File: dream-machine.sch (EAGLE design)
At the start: 8 parts, among them J1 AVR_SPI_PRG_62X3_LOCK, SW1 Now, U1 ATTINY13SOIC

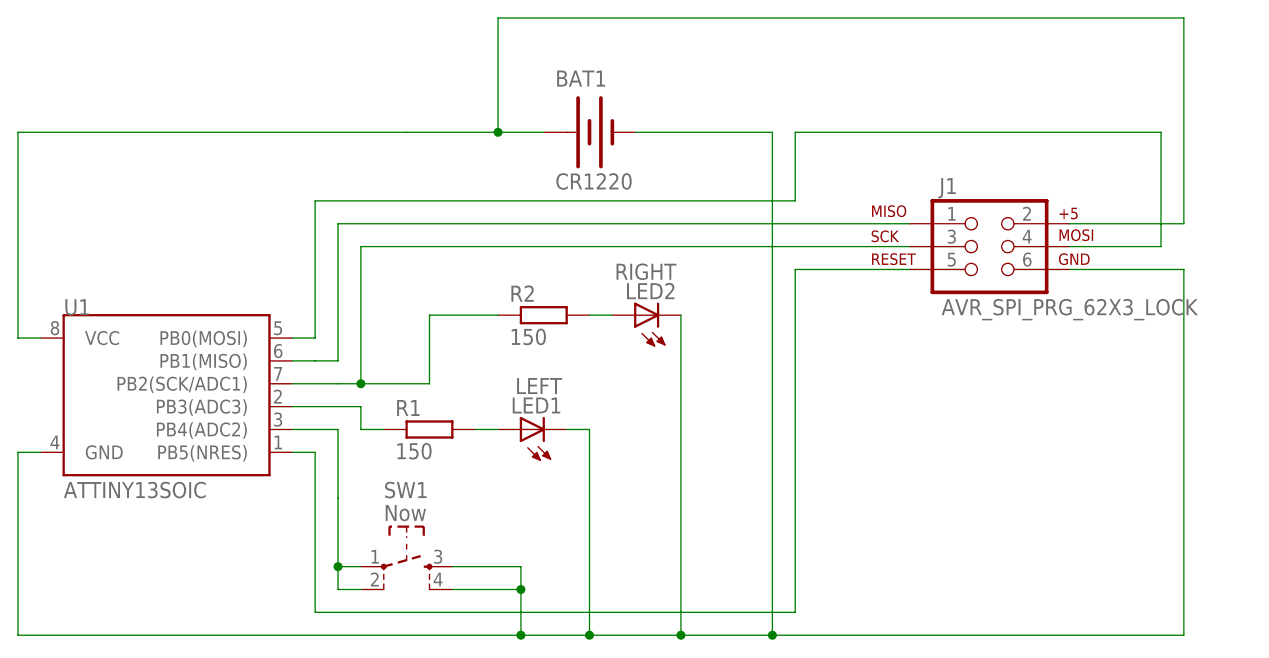
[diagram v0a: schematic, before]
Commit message: Added power jumper. Fixed orientation of battery holder.
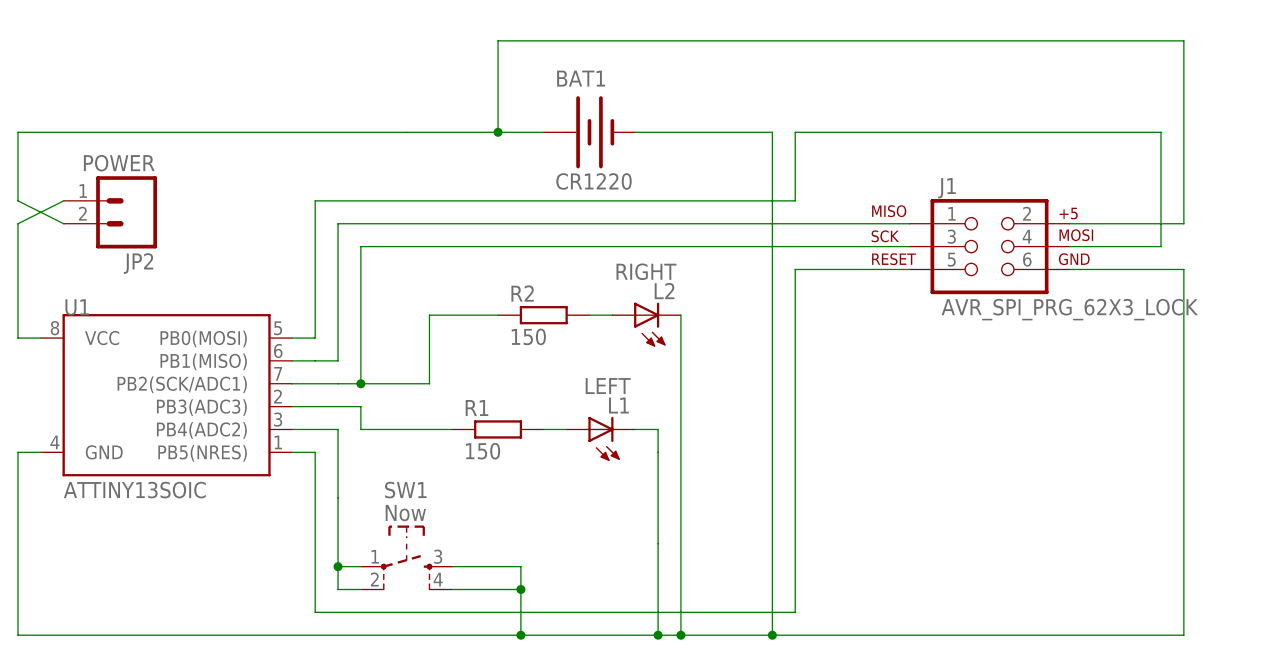
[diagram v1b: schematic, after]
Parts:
- removed LED1: LEFT, dp_devices:LED-3MM
- added JP2: POWER, SparkFun:M02LOCK
- added L1: LEFT, dp_devices:LED-3MM
- renumbered LED2 to L2
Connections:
- new net VCC-POWER: JP2.1, U1.VCC
- net GND: now also L1.C; no longer LED1.C
- net L1-R: now also L1.A; no longer LED1.A
- net VCC: now also JP2.2; no longer U1.VCC
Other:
- moved on the sheet: R1
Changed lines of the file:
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@@
 <part name="U1" library="SparkFun" deviceset="ATTINY13" device="SOIC"/>
 <part name="SW1" library="dp_devices" deviceset="SW_TACT" device="" value="Now"/>
-<part name="LED1" library="dp_devices" deviceset="LED" device="-3MM" value="LEFT"/>
-<part name="LED2" library="dp_devices" deviceset="LED" device="-3MM" value="RIGHT"/>
+<part name="L1" library="dp_devices" deviceset="LED" device="-3MM" value="LEFT"/>
+<part name="L2" library="dp_devices" deviceset="LED" device="-3MM" value="RIGHT"/>
 <part name="R2" library="dp_devices" deviceset="RESISTOR" device="-0805" technology="R805" value="150"/>
 <part name="R1" library="dp_devices" deviceset="RESISTOR" device="-0805" technology="R805" value="150"/>
 <part name="J1" library="SparkFun" deviceset="AVR_SPI_PRG_6" device="2X3_LOCK"/>
+<part name="JP2" library="SparkFun" deviceset="M02" device="LOCK" value="POWER"/>
 </parts>
 <sheets>
@@
 <instance part="U1" gate="G$1" x="27.94" y="35.56"/>
 <instance part="SW1" gate="G$1" x="53.34" y="17.78"/>
-<instance part="LED1" gate="LED" x="66.04" y="33.02" rot="R90"/>
-<instance part="LED2" gate="LED" x="78.74" y="45.72" rot="R90"/>
+<instance part="L1" gate="LED" x="73.66" y="33.02" rot="R90"/>
+<instance part="L2" gate="LED" x="78.74" y="45.72" rot="R90"/>
 <instance part="R2" gate="G$1" x="68.58" y="45.72"/>
-<instance part="R1" gate="G$1" x="55.88" y="33.02"/>
+<instance part="R1" gate="G$1" x="63.5" y="33.02"/>
 <instance part="J1" gate="G$1" x="116.84" y="53.34"/>
+<instance part="JP2" gate="G$1" x="22.86" y="58.42" rot="R180"/>
 </instances>
 <busses>
@@
 <pinref part="BAT1" gate="G$1" pin="+"/>
 <wire x1="68.58" y1="66.04" x2="63.5" y2="66.04" width="0.1524" layer="91"/>
-<pinref part="U1" gate="G$1" pin="VCC"/>
 <wire x1="63.5" y1="66.04" x2="53.34" y2="66.04" width="0.1524" layer="91"/>
-<wire x1="12.7" y1="43.18" x2="10.16" y2="43.18" width="0.1524" layer="91"/>
-<wire x1="10.16" y1="43.18" x2="10.16" y2="66.04" width="0.1524" layer="91"/>
 <wire x1="10.16" y1="66.04" x2="53.34" y2="66.04" width="0.1524" layer="91"/>
-<wire x1="63.5" y1="66.04" x2="63.5" y2="78.74" width="0.1524" layer="91"/>
+<wire x1="63.5" y1="66.04" x2="63.5" y2="76.2" width="0.1524" layer="91"/>
 <junction x="63.5" y="66.04"/>
-<wire x1="63.5" y1="78.74" x2="139.7" y2="78.74" width="0.1524" layer="91"/>
-<wire x1="139.7" y1="78.74" x2="139.7" y2="55.88" width="0.1524" layer="91"/>
+<wire x1="63.5" y1="76.2" x2="139.7" y2="76.2" width="0.1524" layer="91"/>
+<wire x1="139.7" y1="76.2" x2="139.7" y2="55.88" width="0.1524" layer="91"/>
 <pinref part="J1" gate="G$1" pin="2"/>
 <wire x1="139.7" y1="55.88" x2="127" y2="55.88" width="0.1524" layer="91"/>
+<wire x1="10.16" y1="66.04" x2="10.16" y2="58.42" width="0.1524" layer="91"/>
+<pinref part="JP2" gate="G$1" pin="2"/>
+<wire x1="10.16" y1="58.42" x2="15.24" y2="55.88" width="0.1524" layer="91"/>
 </segment>
 </net>
@@
 <wire x1="93.98" y1="66.04" x2="93.98" y2="10.16" width="0.1524" layer="91"/>
 <wire x1="93.98" y1="10.16" x2="83.82" y2="10.16" width="0.1524" layer="91"/>
-<wire x1="83.82" y1="10.16" x2="73.66" y2="10.16" width="0.1524" layer="91"/>
-<wire x1="73.66" y1="10.16" x2="66.04" y2="10.16" width="0.1524" layer="91"/>
+<wire x1="83.82" y1="10.16" x2="81.28" y2="10.16" width="0.1524" layer="91"/>
+<wire x1="81.28" y1="10.16" x2="66.04" y2="10.16" width="0.1524" layer="91"/>
 <wire x1="66.04" y1="10.16" x2="10.16" y2="10.16" width="0.1524" layer="91"/>
 <wire x1="10.16" y1="10.16" x2="10.16" y2="30.48" width="0.1524" layer="91"/>
 <pinref part="U1" gate="G$1" pin="GND"/>
 <wire x1="10.16" y1="30.48" x2="12.7" y2="30.48" width="0.1524" layer="91"/>
-<pinref part="LED2" gate="LED" pin="C"/>
+<pinref part="L2" gate="LED" pin="C"/>
 <wire x1="83.82" y1="45.72" x2="83.82" y2="10.16" width="0.1524" layer="91"/>
-<pinref part="LED1" gate="LED" pin="C"/>
-<wire x1="71.12" y1="33.02" x2="73.66" y2="33.02" width="0.1524" layer="91"/>
-<wire x1="73.66" y1="33.02" x2="73.66" y2="30.48" width="0.1524" layer="91"/>
-<wire x1="73.66" y1="30.48" x2="73.66" y2="20.32" width="0.1524" layer="91"/>
-<wire x1="73.66" y1="20.32" x2="73.66" y2="10.16" width="0.1524" layer="91"/>
-<junction x="73.66" y="10.16"/>
+<pinref part="L1" gate="LED" pin="C"/>
+<wire x1="78.74" y1="33.02" x2="81.28" y2="33.02" width="0.1524" layer="91"/>
+<wire x1="81.28" y1="33.02" x2="81.28" y2="30.48" width="0.1524" layer="91"/>
+<wire x1="81.28" y1="30.48" x2="81.28" y2="20.32" width="0.1524" layer="91"/>
+<wire x1="81.28" y1="20.32" x2="81.28" y2="10.16" width="0.1524" layer="91"/>
+<junction x="81.28" y="10.16"/>
 <pinref part="SW1" gate="G$1" pin="3"/>
 <wire x1="58.42" y1="17.78" x2="66.04" y2="17.78" width="0.1524" layer="91"/>
@@
 <wire x1="40.64" y1="35.56" x2="48.26" y2="35.56" width="0.1524" layer="91"/>
 <wire x1="48.26" y1="35.56" x2="48.26" y2="33.02" width="0.1524" layer="91"/>
-<wire x1="48.26" y1="33.02" x2="50.8" y2="33.02" width="0.1524" layer="91"/>
+<wire x1="48.26" y1="33.02" x2="58.42" y2="33.02" width="0.1524" layer="91"/>
 <pinref part="R1" gate="G$1" pin="1"/>
 </segment>
@@
 <segment>
 <pinref part="R1" gate="G$1" pin="2"/>
-<pinref part="LED1" gate="LED" pin="A"/>
-<wire x1="63.5" y1="33.02" x2="60.96" y2="33.02" width="0.1524" layer="91"/>
+<pinref part="L1" gate="LED" pin="A"/>
+<wire x1="71.12" y1="33.02" x2="68.58" y2="33.02" width="0.1524" layer="91"/>
 </segment>
 </net>
@@
 <segment>
 <pinref part="R2" gate="G$1" pin="2"/>
-<pinref part="LED2" gate="LED" pin="A"/>
+<pinref part="L2" gate="LED" pin="A"/>
 <wire x1="73.66" y1="45.72" x2="76.2" y2="45.72" width="0.1524" layer="91"/>
 </segment>
@@
 </segment>
 </net>
+<net name="VCC-POWER" class="0">
+<segment>
+<pinref part="JP2" gate="G$1" pin="1"/>
+<wire x1="15.24" y1="58.42" x2="10.16" y2="55.88" width="0.1524" layer="91"/>
+<wire x1="10.16" y1="55.88" x2="10.16" y2="43.18" width="0.1524" layer="91"/>
+<pinref part="U1" gate="G$1" pin="VCC"/>
+<wire x1="10.16" y1="43.18" x2="12.7" y2="43.18" width="0.1524" layer="91"/>
+</segment>
+</net>
